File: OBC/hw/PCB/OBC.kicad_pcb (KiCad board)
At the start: 2 copper layers, 96 x 89.9 mm, 17 parts, among them J0 Raspberry_Pi_2_3, J1 Power, J11 RPI_MOUNT1, J12 RPI_MOUNT2, J13 RPI_MOUNT3, J14 RPI_MOUNT4, J2 Terminal_5V0, J3 PICOBLADE1, J4 PICOBLADE2, J5 I2C, J6 I2C, J7 CSP_I2C, J8 Power2, U0 Payload, U1 BMP180-V2, U2 MPU-9250-BREAKOUT-R, U3 XA1110

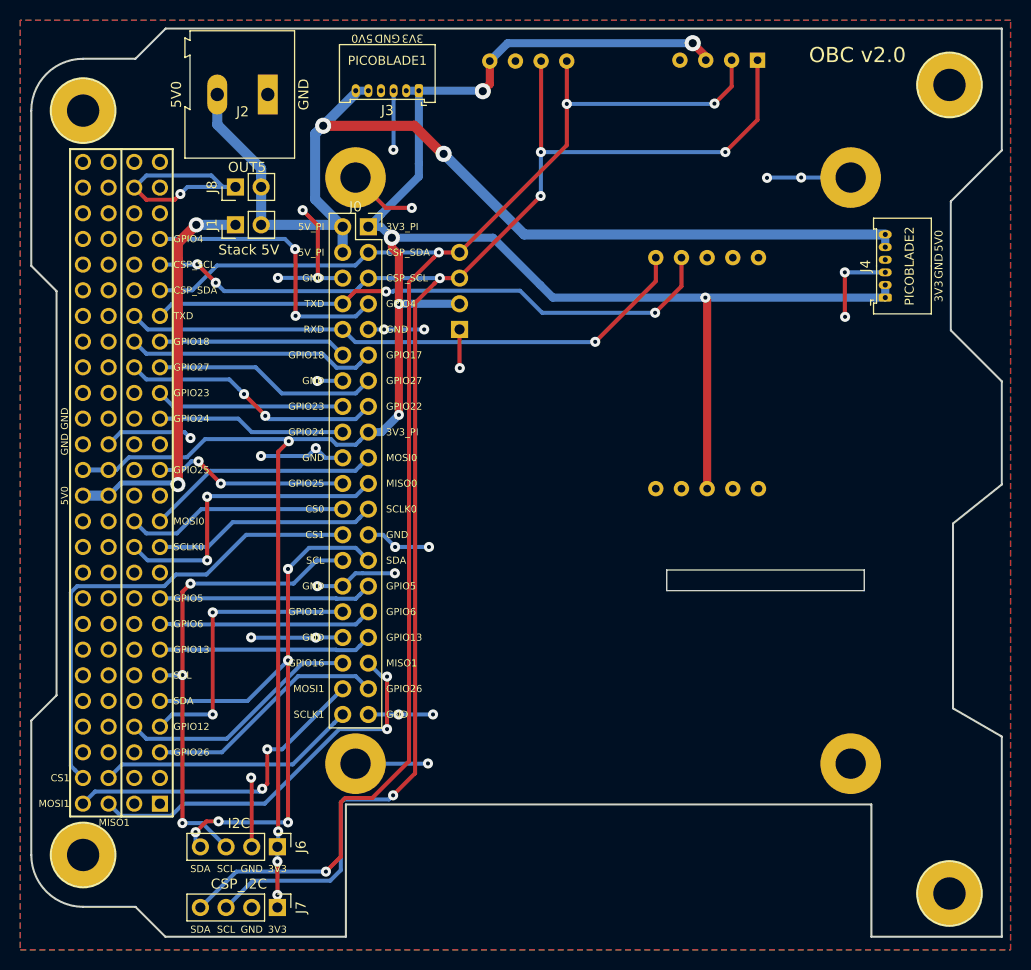
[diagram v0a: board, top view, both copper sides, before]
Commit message: Replaced pin header's footprint with the footprint of the Raspberry pi zero.
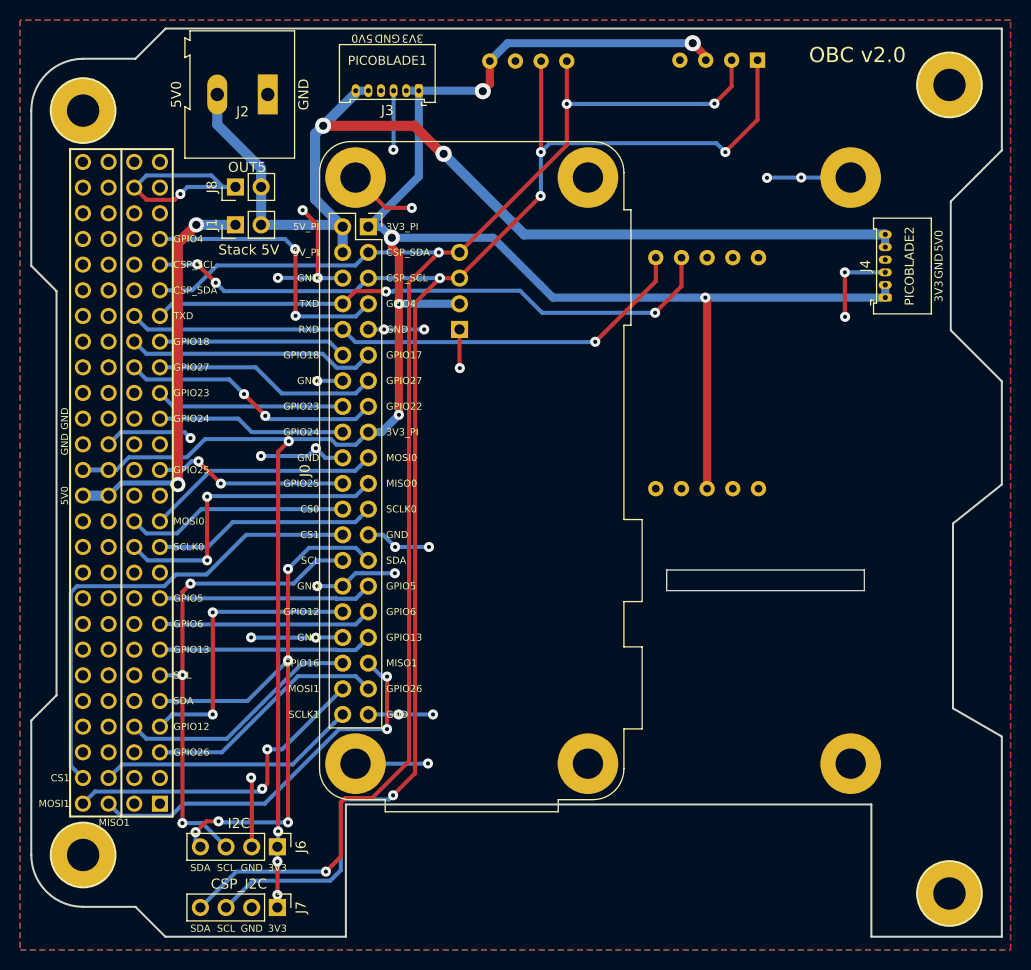
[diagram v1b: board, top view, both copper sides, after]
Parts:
- removed J11: RPI_MOUNT1, Connector_PinHeader_2.54mm:PinHeader_1x01_P2.54mm_Vertical
- removed J12: RPI_MOUNT2, Connector_PinHeader_2.54mm:PinHeader_1x01_P2.54mm_Vertical
- J0: footprint Connector_PinSocket_2.54mm:PinSocket_2x20_P2.54mm_Vertical -> Module:Raspberry_Pi_Zero_Socketed_THT_FaceDown_MountingHoles
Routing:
- net /CSP_SCL: track 162.9 -> 163.7 mm

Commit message: Added the mounting holes for the Raspberry pi zero. Generated new gerber and CAD files.
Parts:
- U2: value MPU-9250-BREAKOUT-R -> MPU-9250
